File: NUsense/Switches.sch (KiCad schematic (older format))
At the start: 6 parts

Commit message: Correct broken files
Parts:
- removed C?: C, symbol C
- removed R?: R, symbol R
- added C?: 0.1uF, symbol C
- added LS?: Speaker, symbol Speaker
- added Q?: 2N3055, TO_SOT_Packages_THT:TO-3, symbol 2N3055
- added R?: 10K, symbol R
- C?: value C -> 0.1uF
- R?: value R -> 10K
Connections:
- net GND: now also C?.2, Q?.2 (E)
- net MCU_NRESET renamed MCU_RESET
- net MCU_RESET: now also R?.2
- net VDD3o3V renamed +3V3
- net +3V3: now also C?.1, LS?.1, R?.1
- new net: LS?.2, Q?.3 (C)
- new net BUZZER_SIG: Q?.1 (B)
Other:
- note added: "Buzzer"
- note added: "System Reset"
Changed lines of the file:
@@
 LIBS:valves
 LIBS:ADM6713RAKS
+LIBS:Header_Connectors
 LIBS:MPU6000
 LIBS:NUbots
@@
 $Descr A3 16535 11693
 encoding utf-8
-Sheet 4 4
+Sheet 4 9
 Title ""
 Date ""
@@
 $Comp
 L C C?
-U 1 1 5A6C0F0D
-P 3000 2400
-F 0 "C?" H 3025 2500 50  0000 L CNN
-F 1 "C" H 3025 2300 50  0000 L CNN
-F 2 "" H 3038 2250 50  0001 C CNN
-F 3 "" H 3000 2400 50  0001 C CNN
-	1    3000 2400
-	1    0    0    -1
-$EndComp
-$Comp
-L C C?
 U 1 1 5A6C0F14
 P 2650 2400
 F 0 "C?" H 2675 2500 50  0000 L CNN
-F 1 "C" H 2675 2300 50  0000 L CNN
+F 1 "0.1uF" H 2675 2300 50  0000 L CNN
 F 2 "" H 2688 2250 50  0001 C CNN
 F 3 "" H 2650 2400 50  0001 C CNN
@@
 P 2650 1800
 F 0 "R?" V 2730 1800 50  0000 C CNN
-F 1 "R" V 2650 1800 50  0000 C CNN
+F 1 "10K" V 2650 1800 50  0000 C CNN
 F 2 "" V 2580 1800 50  0001 C CNN
 F 3 "" H 2650 1800 50  0001 C CNN
@@
 	1    0    0    -1
 $EndComp
-Text GLabel 2650 1400 1    60   Input ~ 0
-VDD3o3V
 Wire Wire Line
 	2650 1400 2650 1650
@@
 	1    0    0    -1
 $EndComp
+Connection ~ 3000 1500
+Wire Wire Line
+	3800 1500 4400 1500
+Wire Wire Line
+	4400 1500 4400 1800
+Wire Wire Line
+	4250 1800 4700 1800
+Wire Wire Line
+	4250 2000 4400 2000
+Wire Wire Line
+	4400 2000 4400 2150
+Connection ~ 4400 1800
+Text Notes 1950 3000 0    60   ~ 0
+System Reset
+$Comp
+L GND #PWR?
+U 1 1 5A6A7F67
+P 1950 4650
+F 0 "#PWR?" H 1950 4400 50  0001 C CNN
+F 1 "GND" H 1950 4500 50  0000 C CNN
+F 2 "" H 1950 4650 50  0001 C CNN
+F 3 "" H 1950 4650 50  0001 C CNN
+	1    1950 4650
+	1    0    0    -1
+$EndComp
+$Comp
+L 2N3055 Q?
+U 1 1 5A6A7F87
+P 1850 4250
+F 0 "Q?" H 2050 4325 50  0000 L CNN
+F 1 "2N3055" H 2050 4250 50  0000 L CNN
+F 2 "TO_SOT_Packages_THT:TO-3" H 2050 4175 50  0001 L CIN
+F 3 "" H 1850 4250 50  0001 L CNN
+	1    1850 4250
+	1    0    0    -1
+$EndComp
+$Comp
+L Speaker LS?
+U 1 1 5A6A7FD9
+P 2400 3750
+F 0 "LS?" H 2450 3975 50  0000 R CNN
+F 1 "Speaker" H 2450 3900 50  0000 R CNN
+F 2 "" H 2400 3550 50  0001 C CNN
+F 3 "" H 2390 3700 50  0001 C CNN
+	1    2400 3750
+	1    0    0    -1
+$EndComp
+Wire Wire Line
+	1350 4250 1650 4250
+Wire Wire Line
+	1950 4050 1950 3850
+Wire Wire Line
+	1950 3850 2200 3850
+Wire Wire Line
+	1950 4650 1950 4450
+Wire Wire Line
+	1950 3650 1950 3750
+Wire Wire Line
+	1950 3750 2200 3750
+Text Notes 1150 4750 0    60   ~ 0
+Buzzer
+$Comp
+L +3.3V #PWR?
+U 1 1 5A6FD90A
+P 2650 1400
+F 0 "#PWR?" H 2650 1250 50  0001 C CNN
+F 1 "+3.3V" H 2650 1540 50  0000 C CNN
+F 2 "" H 2650 1400 50  0001 C CNN
+F 3 "" H 2650 1400 50  0001 C CNN
+	1    2650 1400
+	1    0    0    -1
+$EndComp
+$Comp
+L +3.3V #PWR?
+U 1 1 5A6FD934
+P 1950 3650
+F 0 "#PWR?" H 1950 3500 50  0001 C CNN
+F 1 "+3.3V" H 1950 3790 50  0000 C CNN
+F 2 "" H 1950 3650 50  0001 C CNN
+F 3 "" H 1950 3650 50  0001 C CNN
+	1    1950 3650
+	1    0    0    -1
+$EndComp
+Text HLabel 1350 4250 0    60   Input ~ 0
+BUZZER_SIG
+Text HLabel 4700 1800 2    60   Output ~ 0
+MCU_RESET
+$Comp
+L C C?
+U 1 1 5A704C77
+P 3000 2400
+F 0 "C?" H 3025 2500 50  0000 L CNN
+F 1 "0.1uF" H 3025 2300 50  0000 L CNN
+F 2 "" H 3038 2250 50  0001 C CNN
+F 3 "" H 3000 2400 50  0001 C CNN
+	1    3000 2400
+	1    0    0    -1
+$EndComp
 $Comp
 L R R?
-U 1 1 5A6C0F4F
+U 1 1 5A704CB3
 P 3650 1500
 F 0 "R?" V 3730 1500 50  0000 C CNN
-F 1 "R" V 3650 1500 50  0000 C CNN
+F 1 "10K" V 3650 1500 50  0000 C CNN
 F 2 "" V 3580 1500 50  0001 C CNN
 F 3 "" H 3650 1500 50  0001 C CNN
@@
 	0    -1   -1   0
 $EndComp
-Connection ~ 3000 1500
-Wire Wire Line
-	3800 1500 4400 1500
-Wire Wire Line
-	4400 1500 4400 1800
-Wire Wire Line
-	4250 1800 4700 1800
-Wire Wire Line
-	4250 2000 4400 2000
-Wire Wire Line
-	4400 2000 4400 2150
-Text GLabel 4700 1800 2    60   Input ~ 0
-MCU_NRESET
-Connection ~ 4400 1800
 $EndSCHEMATC

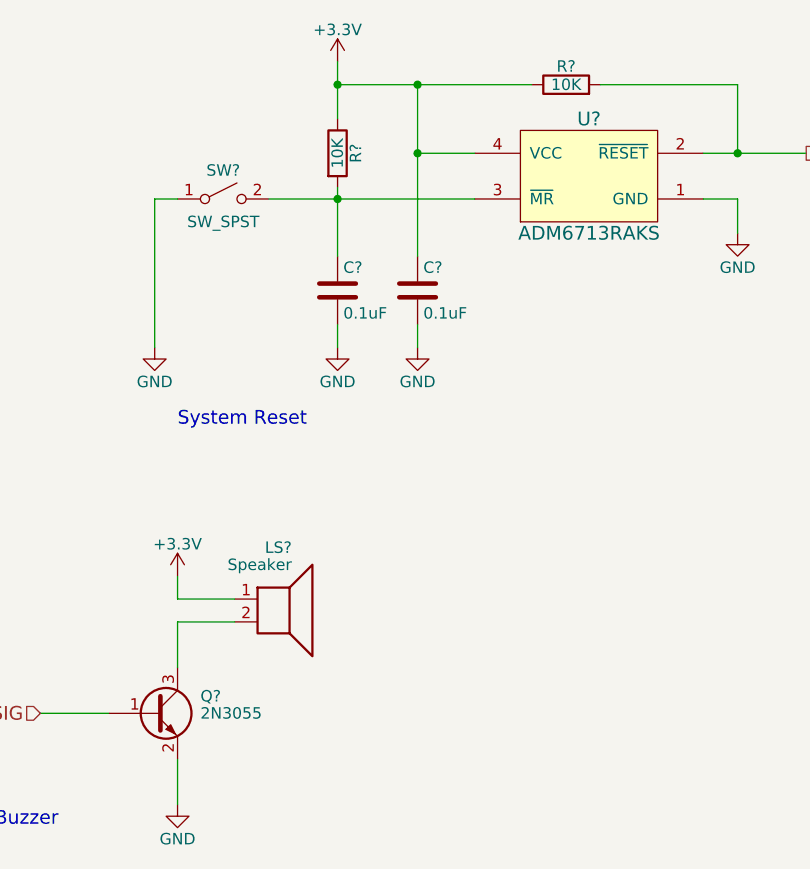
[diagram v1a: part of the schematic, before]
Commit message: Adds annotations and footprints to all components
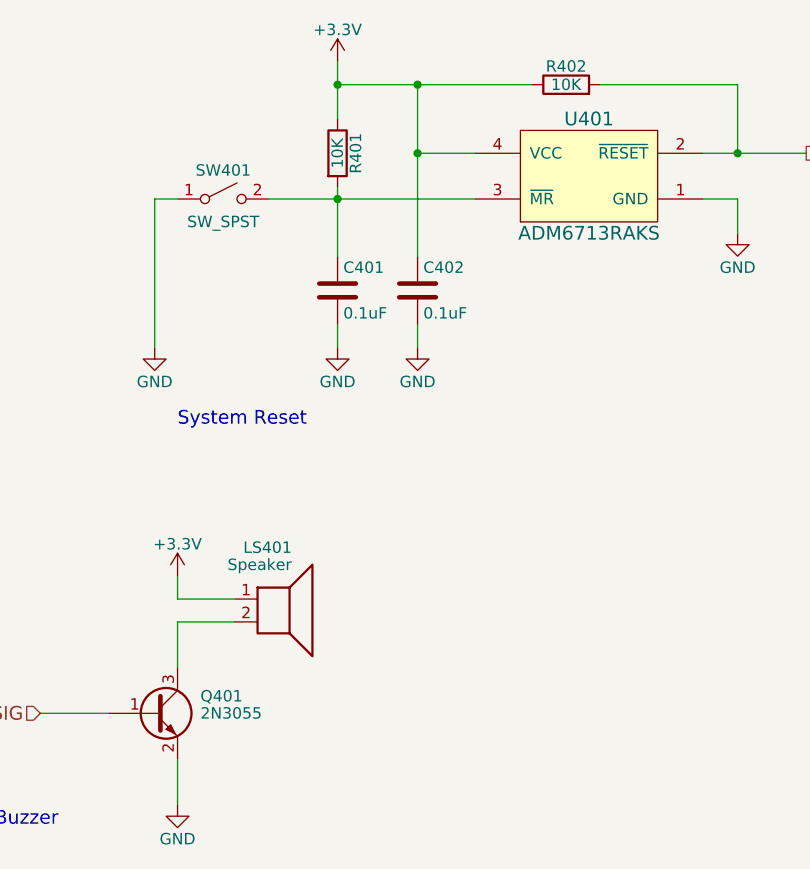
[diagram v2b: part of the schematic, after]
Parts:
- C401, C402: renamed from C?; footprint (none) -> Capacitors_SMD:C_0805_HandSoldering
- Q401: renamed from Q?; footprint TO_SOT_Packages_THT:TO-3 -> TO_SOT_Packages_SMD:SOT-23
- R401, R402: renamed from R?; footprint (none) -> Resistors_SMD:R_0805_HandSoldering
- U401: renamed from U?; footprint (none) -> Footprints:SC82
- gave numbers to parts that had none: 2
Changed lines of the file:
@@
 $Descr A3 16535 11693
 encoding utf-8
-Sheet 4 9
+Sheet 4 12
 Title ""
 Date ""
@@
 $EndDescr
 $Comp
-L ADM6713RAKS U?
+L ADM6713RAKS U401
 U 1 1 5A6C0F06
 P 3450 2100
-F 0 "U?" H 3750 2550 60  0000 C CNN
+F 0 "U401" H 3750 2550 60  0000 C CNN
 F 1 "ADM6713RAKS" H 3750 2050 60  0000 C CNN
-F 2 "" H 3450 2100 60  0001 C CNN
+F 2 "Footprints:SC82" H 3450 2100 60  0001 C CNN
 F 3 "" H 3450 2100 60  0001 C CNN
 	1    3450 2100
@@
 $EndComp
 $Comp
-L C C?
+L C C401
 U 1 1 5A6C0F14
 P 2650 2400
-F 0 "C?" H 2675 2500 50  0000 L CNN
+F 0 "C401" H 2675 2500 50  0000 L CNN
 F 1 "0.1uF" H 2675 2300 50  0000 L CNN
-F 2 "" H 2688 2250 50  0001 C CNN
+F 2 "Capacitors_SMD:C_0805_HandSoldering" H 2688 2250 50  0001 C CNN
 F 3 "" H 2650 2400 50  0001 C CNN
 	1    2650 2400
@@
 $EndComp
 $Comp
-L GND #PWR?
+L GND #PWR405
 U 1 1 5A6C0F1B
 P 2650 2650
-F 0 "#PWR?" H 2650 2400 50  0001 C CNN
+F 0 "#PWR405" H 2650 2400 50  0001 C CNN
 F 1 "GND" H 2650 2500 50  0000 C CNN
 F 2 "" H 2650 2650 50  0001 C CNN
@@
 $EndComp
 $Comp
-L GND #PWR?
+L GND #PWR406
 U 1 1 5A6C0F21
 P 3000 2650
-F 0 "#PWR?" H 3000 2400 50  0001 C CNN
+F 0 "#PWR406" H 3000 2400 50  0001 C CNN
 F 1 "GND" H 3000 2500 50  0000 C CNN
 F 2 "" H 3000 2650 50  0001 C CNN
@@
 $EndComp
 $Comp
-L GND #PWR?
+L GND #PWR401
 U 1 1 5A6C0F27
 P 1850 2650
-F 0 "#PWR?" H 1850 2400 50  0001 C CNN
+F 0 "#PWR401" H 1850 2400 50  0001 C CNN
 F 1 "GND" H 1850 2500 50  0000 C CNN
 F 2 "" H 1850 2650 50  0001 C CNN
@@
 $EndComp
 $Comp
-L SW_SPST SW?
+L SW_SPST SW401
 U 1 1 5A6C0F2D
 P 2150 2000
-F 0 "SW?" H 2150 2125 50  0000 C CNN
+F 0 "SW401" H 2150 2125 50  0000 C CNN
 F 1 "SW_SPST" H 2150 1900 50  0000 C CNN
 F 2 "" H 2150 2000 50  0001 C CNN
@@
 $EndComp
 $Comp
-L R R?
+L R R401
 U 1 1 5A6C0F34
 P 2650 1800
-F 0 "R?" V 2730 1800 50  0000 C CNN
+F 0 "R401" V 2730 1800 50  0000 C CNN
 F 1 "10K" V 2650 1800 50  0000 C CNN
-F 2 "" V 2580 1800 50  0001 C CNN
+F 2 "Resistors_SMD:R_0805_HandSoldering" V 2580 1800 50  0001 C CNN
 F 3 "" H 2650 1800 50  0001 C CNN
 	1    2650 1800
@@
 Connection ~ 2650 1500
 $Comp
-L GND #PWR?
+L GND #PWR407
 U 1 1 5A6C0F49
 P 4400 2150
-F 0 "#PWR?" H 4400 1900 50  0001 C CNN
+F 0 "#PWR407" H 4400 1900 50  0001 C CNN
 F 1 "GND" H 4400 2000 50  0000 C CNN
 F 2 "" H 4400 2150 50  0001 C CNN
@@
 System Reset
 $Comp
-L GND #PWR?
+L GND #PWR403
 U 1 1 5A6A7F67
 P 1950 4650
-F 0 "#PWR?" H 1950 4400 50  0001 C CNN
+F 0 "#PWR403" H 1950 4400 50  0001 C CNN
 F 1 "GND" H 1950 4500 50  0000 C CNN
 F 2 "" H 1950 4650 50  0001 C CNN
@@
 $EndComp
 $Comp
-L 2N3055 Q?
+L 2N3055 Q401
 U 1 1 5A6A7F87
 P 1850 4250
-F 0 "Q?" H 2050 4325 50  0000 L CNN
+F 0 "Q401" H 2050 4325 50  0000 L CNN
 F 1 "2N3055" H 2050 4250 50  0000 L CNN
-F 2 "TO_SOT_Packages_THT:TO-3" H 2050 4175 50  0001 L CIN
+F 2 "TO_SOT_Packages_SMD:SOT-23" H 2050 4175 50  0001 L CIN
 F 3 "" H 1850 4250 50  0001 L CNN
 	1    1850 4250
@@
 $EndComp
 $Comp
-L Speaker LS?
+L Speaker LS401
 U 1 1 5A6A7FD9
 P 2400 3750
-F 0 "LS?" H 2450 3975 50  0000 R CNN
+F 0 "LS401" H 2450 3975 50  0000 R CNN
 F 1 "Speaker" H 2450 3900 50  0000 R CNN
 F 2 "" H 2400 3550 50  0001 C CNN
@@
 Buzzer
 $Comp
-L +3.3V #PWR?
+L +3.3V #PWR404
 U 1 1 5A6FD90A
 P 2650 1400
-F 0 "#PWR?" H 2650 1250 50  0001 C CNN
+F 0 "#PWR404" H 2650 1250 50  0001 C CNN
 F 1 "+3.3V" H 2650 1540 50  0000 C CNN
 F 2 "" H 2650 1400 50  0001 C CNN
@@
 $EndComp
 $Comp
-L +3.3V #PWR?
+L +3.3V #PWR402
 U 1 1 5A6FD934
 P 1950 3650
-F 0 "#PWR?" H 1950 3500 50  0001 C CNN
+F 0 "#PWR402" H 1950 3500 50  0001 C CNN
 F 1 "+3.3V" H 1950 3790 50  0000 C CNN
 F 2 "" H 1950 3650 50  0001 C CNN
@@
 MCU_RESET
 $Comp
-L C C?
+L C C402
 U 1 1 5A704C77
 P 3000 2400
-F 0 "C?" H 3025 2500 50  0000 L CNN
+F 0 "C402" H 3025 2500 50  0000 L CNN
 F 1 "0.1uF" H 3025 2300 50  0000 L CNN
-F 2 "" H 3038 2250 50  0001 C CNN
+F 2 "Capacitors_SMD:C_0805_HandSoldering" H 3038 2250 50  0001 C CNN
 F 3 "" H 3000 2400 50  0001 C CNN
 	1    3000 2400
@@
 $EndComp
 $Comp
-L R R?
+L R R402
 U 1 1 5A704CB3
 P 3650 1500
-F 0 "R?" V 3730 1500 50  0000 C CNN
+F 0 "R402" V 3730 1500 50  0000 C CNN
 F 1 "10K" V 3650 1500 50  0000 C CNN
-F 2 "" V 3580 1500 50  0001 C CNN
+F 2 "Resistors_SMD:R_0805_HandSoldering" V 3580 1500 50  0001 C CNN
 F 3 "" H 3650 1500 50  0001 C CNN
 	1    3650 1500

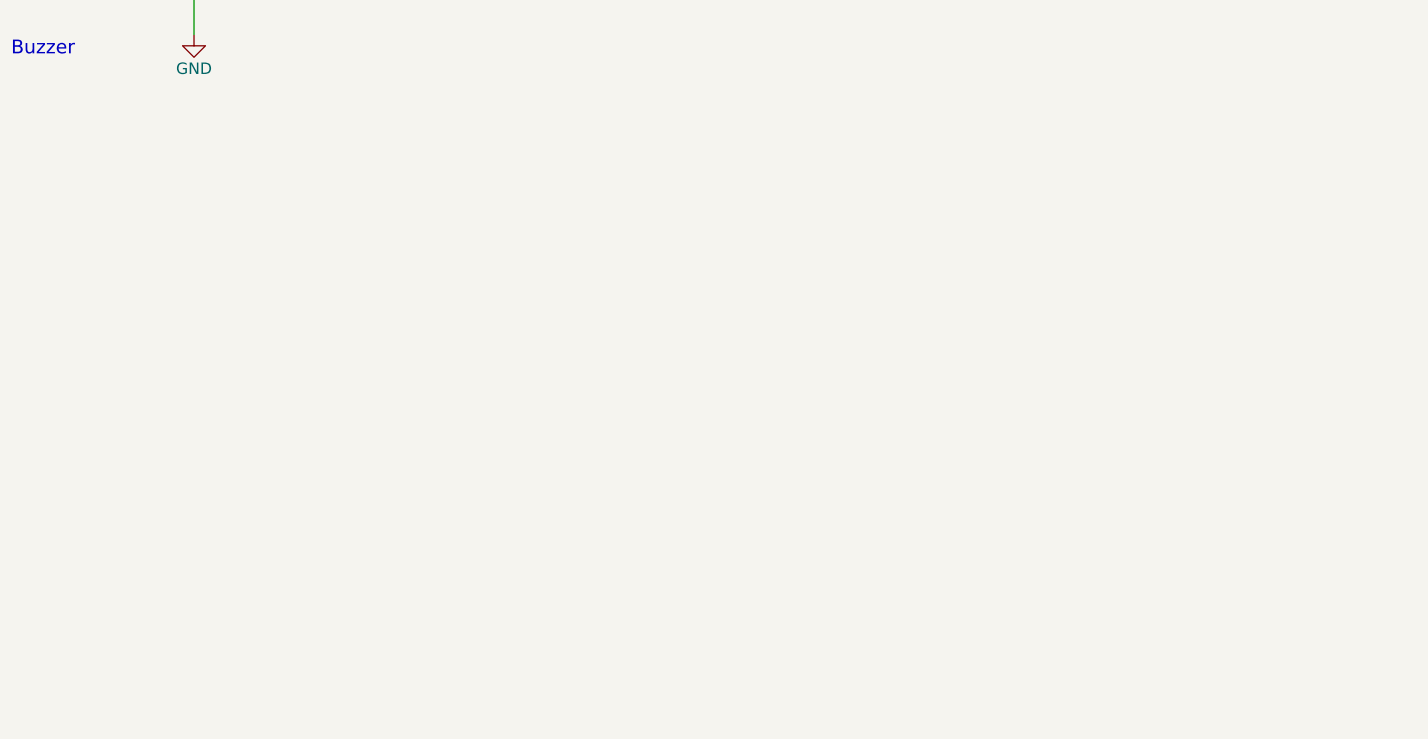
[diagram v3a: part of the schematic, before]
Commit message: Fan PWM
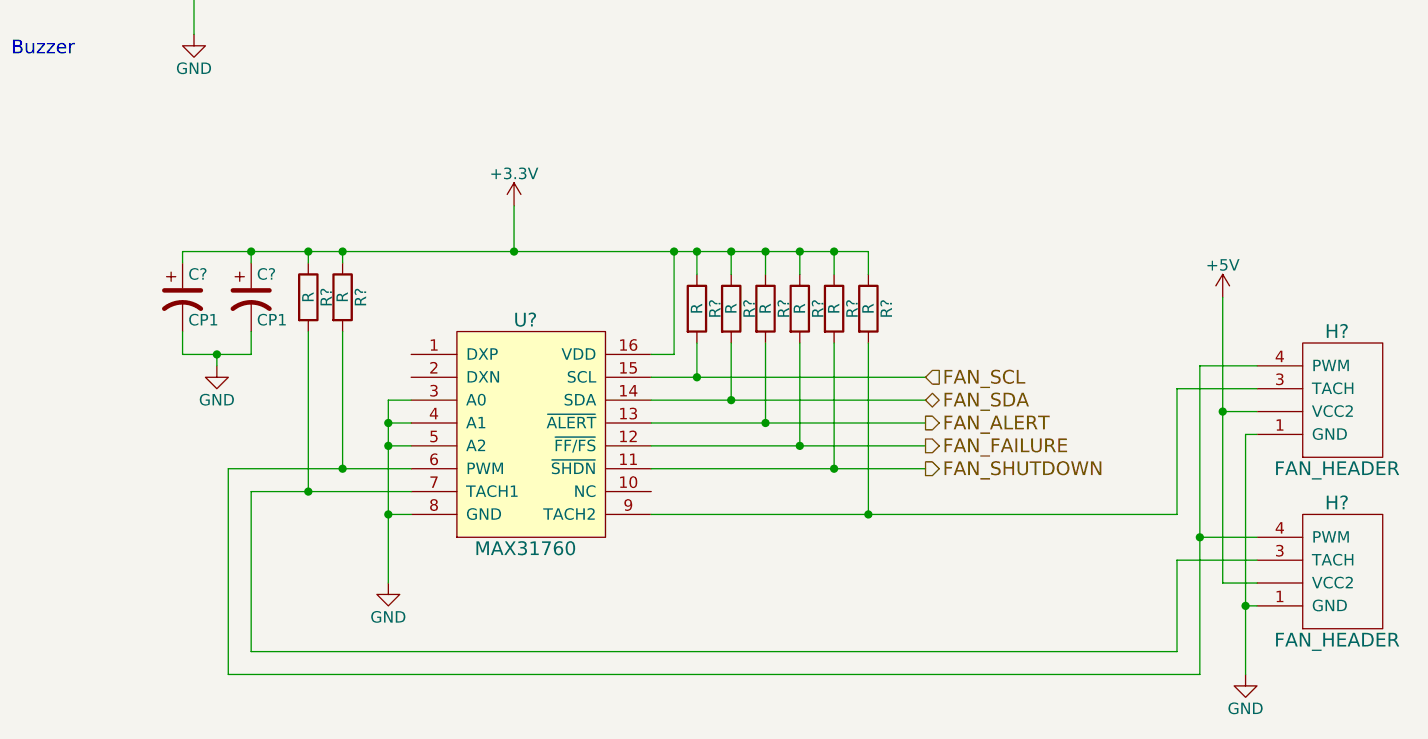
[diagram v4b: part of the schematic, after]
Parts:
- added C? (x2): CP1, symbol CP1
- added H? (x2): FAN_HEADER, symbol FAN_HEADER
- added R? (x8): R, symbol R
- added U?: MAX31760, symbol MAX31760
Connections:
- net +3V3: now also C?.1, C?.1, R?.1, R?.1, R?.1, R?.1, R?.1, R?.1, R?.1, R?.1, U?.16 (VDD)
- net GND: now also C?.2, C?.2, H?.1 (GND), H?.1 (GND), U?.3 (A0), U?.4 (A1), U?.5 (A2), U?.8 (GND)
- new net: H?.4 (PWM), H?.4 (PWM), R?.2, U?.6 (PWM)
- new net: H?.3 (TACH), R?.2, U?.7 (TACH1)
- new net: H?.3 (TACH), R?.2, U?.9 (TACH2)
- new net +5V: H?.~ (VCC2), H?.~ (VCC2)
- new net FAN_ALERT: R?.2, U?.13 (~ALERT)
- new net FAN_FAILURE: R?.2, U?.12 (~FF/FS)
- new net FAN_SCL: R?.2, U?.15 (SCL)
- new net FAN_SDA: R?.2, U?.14 (SDA)
- new net FAN_SHUTDOWN: R?.2, U?.11 (~SHDN)

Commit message: Footprint Fan PWM
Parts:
- U?: footprint (none) -> Footprints:QSOP16
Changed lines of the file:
@@
 F 0 "U?" H 3400 7800 60  0000 C CNN
 F 1 "MAX31760" H 3400 6800 60  0000 C CNN
-F 2 "" H 3100 6850 60  0001 C CNN
+F 2 "Footprints:QSOP16" H 3100 6850 60  0001 C CNN
 F 3 "" H 3100 6850 60  0001 C CNN
 	1    3100 6850
